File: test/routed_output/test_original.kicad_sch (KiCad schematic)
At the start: 3 parts, among them U1 CP_Radial_D25.0mm_P10.00mm_Sn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, U2 R_Axial_DIN0207_L6.3mm_D2.5mm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, U3 R_Axial_DIN0207_L6.3mm_D2.5mm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

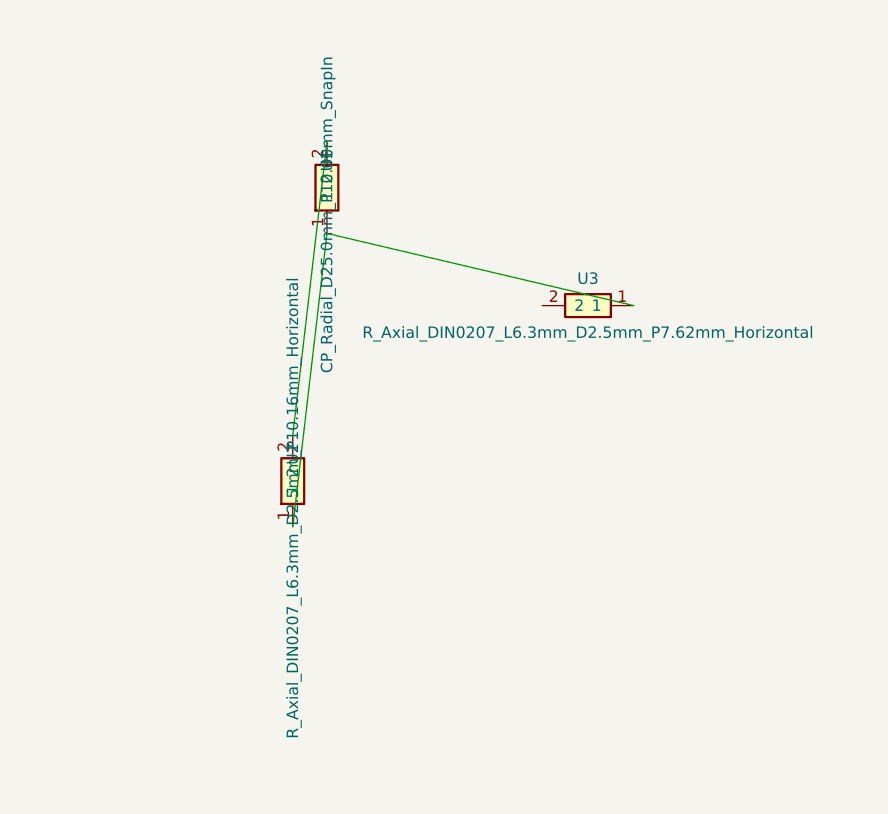
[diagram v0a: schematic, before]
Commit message: fix: schematic router - pin_map mapping + rotation formula alignment
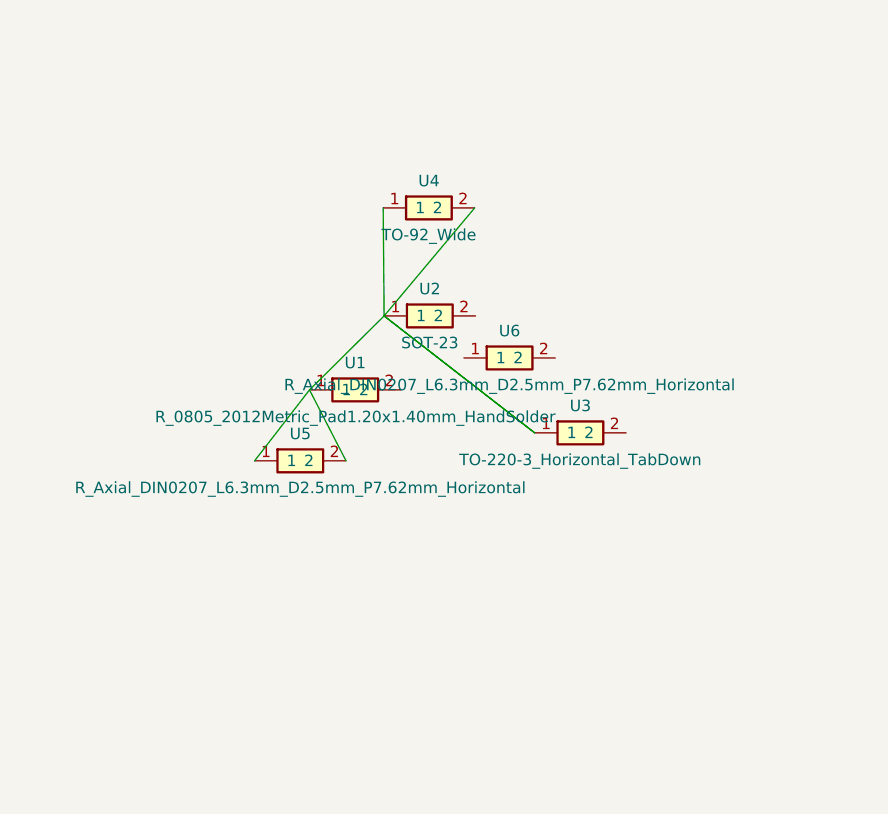
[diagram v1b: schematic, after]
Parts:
- removed U1: CP_Radial_D25.0mm_P10.00mm_SnapIn, 00_basic:CP_Radial_D25.0mm_P10.00mm_SnapIn, symbol 00_basic:C_Polarized
- removed U2: R_Axial_DIN0207_L6.3mm_D2.5mm_P10.16mm_Horizontal, 00_basic:R_Axial_DIN0207_L6.3mm_D2.5mm_P10.16mm_Horizontal, symbol 00_basic:R
- removed U3: R_Axial_DIN0207_L6.3mm_D2.5mm_P7.62mm_Horizontal, 00_basic:R_Axial_DIN0207_L6.3mm_D2.5mm_P7.62mm_Horizontal, symbol _placeholder:U3
- added U1: R_0805_2012Metric_Pad1.20x1.40mm_HandSolder, 00_basic:R_0805_2012Metric_Pad1.20x1.40mm_HandSolder, symbol RE_passive:R
- added U2: SOT-23, RE_active:SOT-23, symbol RE_active:Q_NPN
- added U3: TO-220-3_Horizontal_TabDown, RE_active:TO-220-3_Horizontal_TabDown, symbol RE_active:Q_NMOS
- added U4: TO-92_Wide, RE_active:TO-92_Wide, symbol RE_active:Q_NPN
- added U5: R_Axial_DIN0207_L6.3mm_D2.5mm_P7.62mm_Horizontal, RE_passive_tht:R_Axial_DIN0207_L6.3mm_D2.5mm_P7.62mm_Horizontal, symbol _placeholder:U5
- added U6: R_Axial_DIN0207_L6.3mm_D2.5mm_P7.62mm_Horizontal, RE_passive_tht:R_Axial_DIN0207_L6.3mm_D2.5mm_P7.62mm_Horizontal, symbol _placeholder:U6
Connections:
- new net: U1.1, U2.1, U3.1, U4.1, U4.2, U5.1, U5.2
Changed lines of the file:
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@@
   (paper "A4")
   (symbol
-    (lib_id "00_basic:C_Polarized")
-    (at 135.90 88.70 90)
+    (lib_id "RE_passive:R")
+    (at 139.04 111.17 0)
     (unit 1)
     (exclude_from_sim no)
@@
     (on_board yes)
     (dnp no)
-    (property "Reference" "U1" (at 135.90 85.70 0)
+    (property "Reference" "U1" (at 139.04 108.17 0)
       (effects (font (size 1.27 1.27)))
     )
-    (property "Value" "CP_Radial_D25.0mm_P10.00mm_SnapIn" (at 135.90 91.70 0)
+    (property "Value" "R_0805_2012Metric_Pad1.20x1.40mm_HandSolder" (at 139.04 114.17 0)
       (effects (font (size 1.27 1.27)))
     )
-    (property "Footprint" "00_basic:CP_Radial_D25.0mm_P10.00mm_SnapIn" (at 135.90 93.70 0)
+    (property "Footprint" "00_basic:R_0805_2012Metric_Pad1.20x1.40mm_HandSolder" (at 139.04 116.17 0)
       (effects (font (size 1.27 1.27)) hide)
     )
@@
   )
   (symbol
-    (lib_id "00_basic:R")
-    (at 132.10 121.30 90)
+    (lib_id "RE_active:Q_NPN")
+    (at 147.33 102.95 0)
     (unit 1)
     (exclude_from_sim no)
@@
     (on_board yes)
     (dnp no)
-    (property "Reference" "U2" (at 132.10 118.30 0)
+    (property "Reference" "U2" (at 147.33 99.95 0)
       (effects (font (size 1.27 1.27)))
     )
-    (property "Value" "R_Axial_DIN0207_L6.3mm_D2.5mm_P10.16mm_Horizontal" (at 132.10 124.30 0)
+    (property "Value" "SOT-23" (at 147.33 105.95 0)
       (effects (font (size 1.27 1.27)))
     )
-    (property "Footprint" "00_basic:R_Axial_DIN0207_L6.3mm_D2.5mm_P10.16mm_Horizontal" (at 132.10 126.30 0)
+    (property "Footprint" "RE_active:SOT-23" (at 147.33 107.95 0)
       (effects (font (size 1.27 1.27)) hide)
     )
@@
   )
   (symbol
-    (lib_id "_placeholder:U3")
-    (at 164.90 101.80 180)
+    (lib_id "RE_active:Q_NMOS")
+    (at 164.06 115.94 0)
     (unit 1)
     (exclude_from_sim no)
@@
     (on_board yes)
     (dnp no)
-    (property "Reference" "U3" (at 164.90 98.80 0)
+    (property "Reference" "U3" (at 164.06 112.94 0)
       (effects (font (size 1.27 1.27)))
     )
-    (property "Value" "R_Axial_DIN0207_L6.3mm_D2.5mm_P7.62mm_Horizontal" (at 164.90 104.80 0)
+    (property "Value" "TO-220-3_Horizontal_TabDown" (at 164.06 118.94 0)
       (effects (font (size 1.27 1.27)))
     )
-    (property "Footprint" "00_basic:R_Axial_DIN0207_L6.3mm_D2.5mm_P7.62mm_Horizontal" (at 164.90 106.80 0)
+    (property "Footprint" "RE_active:TO-220-3_Horizontal_TabDown" (at 164.06 120.94 0)
       (effects (font (size 1.27 1.27)) hide)
     )
@@
     )
   )
-  (wire (pts (xy 132.10 126.38) (xy 135.90 93.78))
+  (symbol
+    (lib_id "RE_active:Q_NPN")
+    (at 147.23 90.95 0)
+    (unit 1)
+    (exclude_from_sim no)
+    (in_bom yes)
+    (on_board yes)
+    (dnp no)
+    (property "Reference" "U4" (at 147.23 87.95 0)
+      (effects (font (size 1.27 1.27)))
+    )
+    (property "Value" "TO-92_Wide" (at 147.23 93.95 0)
+      (effects (font (size 1.27 1.27)))
+    )
+    (property "Footprint" "RE_active:TO-92_Wide" (at 147.23 95.95 0)
+      (effects (font (size 1.27 1.27)) hide)
+    )
+    (instances
+      (project ""
+        (path "/"
+          (reference "U4")
+          (unit 1)
+        )
+      )
+    )
+  )
+  (symbol
+    (lib_id "_placeholder:U5")
+    (at 132.94 119.05 0)
+    (unit 1)
+    (exclude_from_sim no)
+    (in_bom yes)
+    (on_board yes)
+    (dnp no)
+    (property "Reference" "U5" (at 132.94 116.05 0)
+      (effects (font (size 1.27 1.27)))
+    )
+    (property "Value" "R_Axial_DIN0207_L6.3mm_D2.5mm_P7.62mm_Horizontal" (at 132.94 122.05 0)
+      (effects (font (size 1.27 1.27)))
+    )
+    (property "Footprint" "RE_passive_tht:R_Axial_DIN0207_L6.3mm_D2.5mm_P7.62mm_Horizontal" (at 132.94 124.05 0)
+      (effects (font (size 1.27 1.27)) hide)
+    )
+    (instances
+      (project ""
+        (path "/"
+          (reference "U5")
+          (unit 1)
+        )
+      )
+    )
+  )
+  (symbol
+    (lib_id "_placeholder:U6")
+    (at 156.19 107.62 0)
+    (unit 1)
+    (exclude_from_sim no)
+    (in_bom yes)
+    (on_board yes)
+    (dnp no)
+    (property "Reference" "U6" (at 156.19 104.62 0)
+      (effects (font (size 1.27 1.27)))
+    )
+    (property "Value" "R_Axial_DIN0207_L6.3mm_D2.5mm_P7.62mm_Horizontal" (at 156.19 110.62 0)
+      (effects (font (size 1.27 1.27)))
+    )
+    (property "Footprint" "RE_passive_tht:R_Axial_DIN0207_L6.3mm_D2.5mm_P7.62mm_Horizontal" (at 156.19 112.62 0)
+      (effects (font (size 1.27 1.27)) hide)
+    )
+    (instances
+      (project ""
+        (path "/"
+          (reference "U6")
+          (unit 1)
+        )
+      )
+    )
+  )
+  (wire (pts (xy 152.31 90.95) (xy 142.25 102.95))
     (stroke (width 0) (type default))
   )
-  (wire (pts (xy 132.10 116.22) (xy 135.90 83.62))
+  (wire (pts (xy 142.25 102.95) (xy 158.98 115.94))
     (stroke (width 0) (type default))
   )
-  (wire (pts (xy 135.90 93.78) (xy 169.98 101.80))
+  (wire (pts (xy 142.25 102.95) (xy 158.98 115.94))
     (stroke (width 0) (type default))
   )
+  (wire (pts (xy 142.25 102.95) (xy 142.15 90.95))
+    (stroke (width 0) (type default))
+  )
+  (wire (pts (xy 133.96 111.17) (xy 142.25 102.95))
+    (stroke (width 0) (type default))
+  )
+  (wire (pts (xy 133.96 111.17) (xy 127.86 119.05))
+    (stroke (width 0) (type default))
+  )
+  (wire (pts (xy 133.96 111.17) (xy 138.02 119.05))
+    (stroke (width 0) (type default))
+  )

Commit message: backup
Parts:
- added U7: CP_Radial_D30.0mm_P10.00mm_SnapIn, RE_passive_tht:CP_Radial_D30.0mm_P10.00mm_SnapIn, symbol RE_passive:C_Polarized
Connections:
- net at U3.2: now also U7.2
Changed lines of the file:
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@@
   (symbol
     (lib_id "RE_passive:R")
-    (at 139.04 111.17 0)
-    (unit 1)
-    (exclude_from_sim no)
-    (in_bom yes)
-    (on_board yes)
-    (dnp no)
-    (property "Reference" "U1" (at 139.04 108.17 0)
-      (effects (font (size 1.27 1.27)))
-    )
-    (property "Value" "R_0805_2012Metric_Pad1.20x1.40mm_HandSolder" (at 139.04 114.17 0)
-      (effects (font (size 1.27 1.27)))
-    )
-    (property "Footprint" "00_basic:R_0805_2012Metric_Pad1.20x1.40mm_HandSolder" (at 139.04 116.17 0)
-      (effects (font (size 1.27 1.27)) hide)
-    )
-    (instances
-      (project ""
-        (path "/"
+    (at 139.04 127.96 0)
+    (unit 1)
+    (exclude_from_sim no)
+    (in_bom yes)
+    (on_board yes)
+    (dnp no)
+    (property "Reference" "U1" (at 139.04 124.96 0)
+      (effects (font (size 1.27 1.27)))
+    )
+    (property "Value" "R_0805_2012Metric_Pad1.20x1.40mm_HandSolder" (at 139.04 130.96 0)
+      (effects (font (size 1.27 1.27)))
+    )
+    (property "Footprint" "00_basic:R_0805_2012Metric_Pad1.20x1.40mm_HandSolder" (at 139.04 132.96 0)
+      (effects (font (size 1.27 1.27)) hide)
+    )
+    (instances
+      (project ""
+        (path "/76b0d100-f5a4-4cb0-a1b7-3defec0bed4b"
           (reference "U1")
           (unit 1)
@@
   (symbol
     (lib_id "RE_active:Q_NPN")
-    (at 147.33 102.95 0)
-    (unit 1)
-    (exclude_from_sim no)
-    (in_bom yes)
-    (on_board yes)
-    (dnp no)
-    (property "Reference" "U2" (at 147.33 99.95 0)
-      (effects (font (size 1.27 1.27)))
-    )
-    (property "Value" "SOT-23" (at 147.33 105.95 0)
-      (effects (font (size 1.27 1.27)))
-    )
-    (property "Footprint" "RE_active:SOT-23" (at 147.33 107.95 0)
-      (effects (font (size 1.27 1.27)) hide)
-    )
-    (instances
-      (project ""
-        (path "/"
+    (at 147.33 119.74 0)
+    (unit 1)
+    (exclude_from_sim no)
+    (in_bom yes)
+    (on_board yes)
+    (dnp no)
+    (property "Reference" "U2" (at 147.33 116.74 0)
+      (effects (font (size 1.27 1.27)))
+    )
+    (property "Value" "SOT-23" (at 147.33 122.74 0)
+      (effects (font (size 1.27 1.27)))
+    )
+    (property "Footprint" "RE_active:SOT-23" (at 147.33 124.74 0)
+      (effects (font (size 1.27 1.27)) hide)
+    )
+    (instances
+      (project ""
+        (path "/76b0d100-f5a4-4cb0-a1b7-3defec0bed4b"
           (reference "U2")
           (unit 1)
@@
   (symbol
     (lib_id "RE_active:Q_NMOS")
-    (at 164.06 115.94 0)
-    (unit 1)
-    (exclude_from_sim no)
-    (in_bom yes)
-    (on_board yes)
-    (dnp no)
-    (property "Reference" "U3" (at 164.06 112.94 0)
-      (effects (font (size 1.27 1.27)))
-    )
-    (property "Value" "TO-220-3_Horizontal_TabDown" (at 164.06 118.94 0)
-      (effects (font (size 1.27 1.27)))
-    )
-    (property "Footprint" "RE_active:TO-220-3_Horizontal_TabDown" (at 164.06 120.94 0)
-      (effects (font (size 1.27 1.27)) hide)
-    )
-    (instances
-      (project ""
-        (path "/"
+    (at 164.06 132.73 0)
+    (unit 1)
+    (exclude_from_sim no)
+    (in_bom yes)
+    (on_board yes)
+    (dnp no)
+    (property "Reference" "U3" (at 164.06 129.73 0)
+      (effects (font (size 1.27 1.27)))
+    )
+    (property "Value" "TO-220-3_Horizontal_TabDown" (at 164.06 135.73 0)
+      (effects (font (size 1.27 1.27)))
+    )
+    (property "Footprint" "RE_active:TO-220-3_Horizontal_TabDown" (at 164.06 137.73 0)
+      (effects (font (size 1.27 1.27)) hide)
+    )
+    (instances
+      (project ""
+        (path "/76b0d100-f5a4-4cb0-a1b7-3defec0bed4b"
           (reference "U3")
           (unit 1)
@@
   (symbol
     (lib_id "RE_active:Q_NPN")
-    (at 147.23 90.95 0)
-    (unit 1)
-    (exclude_from_sim no)
-    (in_bom yes)
-    (on_board yes)
-    (dnp no)
-    (property "Reference" "U4" (at 147.23 87.95 0)
-      (effects (font (size 1.27 1.27)))
-    )
-    (property "Value" "TO-92_Wide" (at 147.23 93.95 0)
-      (effects (font (size 1.27 1.27)))
-    )
-    (property "Footprint" "RE_active:TO-92_Wide" (at 147.23 95.95 0)
-      (effects (font (size 1.27 1.27)) hide)
-    )
-    (instances
-      (project ""
-        (path "/"
+    (at 147.23 107.75 0)
+    (unit 1)
+    (exclude_from_sim no)
+    (in_bom yes)
+    (on_board yes)
+    (dnp no)
+    (property "Reference" "U4" (at 147.23 104.75 0)
+      (effects (font (size 1.27 1.27)))
+    )
+    (property "Value" "TO-92_Wide" (at 147.23 110.75 0)
+      (effects (font (size 1.27 1.27)))
+    )
+    (property "Footprint" "RE_active:TO-92_Wide" (at 147.23 112.75 0)
+      (effects (font (size 1.27 1.27)) hide)
+    )
+    (instances
+      (project ""
+        (path "/76b0d100-f5a4-4cb0-a1b7-3defec0bed4b"
           (reference "U4")
           (unit 1)
@@
   (symbol
     (lib_id "_placeholder:U5")
-    (at 132.94 119.05 0)
-    (unit 1)
-    (exclude_from_sim no)
-    (in_bom yes)
-    (on_board yes)
-    (dnp no)
-    (property "Reference" "U5" (at 132.94 116.05 0)
-      (effects (font (size 1.27 1.27)))
-    )
-    (property "Value" "R_Axial_DIN0207_L6.3mm_D2.5mm_P7.62mm_Horizontal" (at 132.94 122.05 0)
-      (effects (font (size 1.27 1.27)))
-    )
-    (property "Footprint" "RE_passive_tht:R_Axial_DIN0207_L6.3mm_D2.5mm_P7.62mm_Horizontal" (at 132.94 124.05 0)
-      (effects (font (size 1.27 1.27)) hide)
-    )
-    (instances
-      (project ""
-        (path "/"
+    (at 132.94 135.84 0)
+    (unit 1)
+    (exclude_from_sim no)
+    (in_bom yes)
+    (on_board yes)
+    (dnp no)
+    (property "Reference" "U5" (at 132.94 132.84 0)
+      (effects (font (size 1.27 1.27)))
+    )
+    (property "Value" "R_Axial_DIN0207_L6.3mm_D2.5mm_P7.62mm_Horizontal" (at 132.94 138.84 0)
+      (effects (font (size 1.27 1.27)))
+    )
+    (property "Footprint" "RE_passive_tht:R_Axial_DIN0207_L6.3mm_D2.5mm_P7.62mm_Horizontal" (at 132.94 140.84 0)
+      (effects (font (size 1.27 1.27)) hide)
+    )
+    (instances
+      (project ""
+        (path "/76b0d100-f5a4-4cb0-a1b7-3defec0bed4b"
           (reference "U5")
           (unit 1)
@@
   (symbol
     (lib_id "_placeholder:U6")
-    (at 156.19 107.62 0)
-    (unit 1)
-    (exclude_from_sim no)
-    (in_bom yes)
-    (on_board yes)
-    (dnp no)
-    (property "Reference" "U6" (at 156.19 104.62 0)
-      (effects (font (size 1.27 1.27)))
-    )
-    (property "Value" "R_Axial_DIN0207_L6.3mm_D2.5mm_P7.62mm_Horizontal" (at 156.19 110.62 0)
-      (effects (font (size 1.27 1.27)))
-    )
-    (property "Footprint" "RE_passive_tht:R_Axial_DIN0207_L6.3mm_D2.5mm_P7.62mm_Horizontal" (at 156.19 112.62 0)
-      (effects (font (size 1.27 1.27)) hide)
-    )
-    (instances
-      (project ""
-        (path "/"
+    (at 156.19 124.41 0)
+    (unit 1)
+    (exclude_from_sim no)
+    (in_bom yes)
+    (on_board yes)
+    (dnp no)
+    (property "Reference" "U6" (at 156.19 121.41 0)
+      (effects (font (size 1.27 1.27)))
+    )
+    (property "Value" "R_Axial_DIN0207_L6.3mm_D2.5mm_P7.62mm_Horizontal" (at 156.19 127.41 0)
+      (effects (font (size 1.27 1.27)))
+    )
+    (property "Footprint" "RE_passive_tht:R_Axial_DIN0207_L6.3mm_D2.5mm_P7.62mm_Horizontal" (at 156.19 129.41 0)
+      (effects (font (size 1.27 1.27)) hide)
+    )
+    (instances
+      (project ""
+        (path "/76b0d100-f5a4-4cb0-a1b7-3defec0bed4b"
           (reference "U6")
           (unit 1)
@@
     )
   )
-  (wire (pts (xy 152.31 90.95) (xy 142.25 102.95))
-    (stroke (width 0) (type default))
-  )
-  (wire (pts (xy 142.25 102.95) (xy 158.98 115.94))
-    (stroke (width 0) (type default))
-  )
-  (wire (pts (xy 142.25 102.95) (xy 158.98 115.94))
-    (stroke (width 0) (type default))
-  )
-  (wire (pts (xy 142.25 102.95) (xy 142.15 90.95))
-    (stroke (width 0) (type default))
-  )
-  (wire (pts (xy 133.96 111.17) (xy 142.25 102.95))
-    (stroke (width 0) (type default))
-  )
-  (wire (pts (xy 133.96 111.17) (xy 127.86 119.05))
-    (stroke (width 0) (type default))
-  )
-  (wire (pts (xy 133.96 111.17) (xy 138.02 119.05))
-    (stroke (width 0) (type default))
-  )
+  (symbol
+    (lib_id "RE_passive:C_Polarized")
+    (at 157.54 74.16 0)
+    (unit 1)
+    (exclude_from_sim no)
+    (in_bom yes)
+    (on_board yes)
+    (dnp no)
+    (property "Reference" "U7" (at 157.54 71.16 0)
+      (effects (font (size 1.27 1.27)))
+    )
+    (property "Value" "CP_Radial_D30.0mm_P10.00mm_SnapIn" (at 157.54 77.16 0)
+      (effects (font (size 1.27 1.27)))
+    )
+    (property "Footprint" "RE_passive_tht:CP_Radial_D30.0mm_P10.00mm_SnapIn" (at 157.54 79.16 0)
+      (effects (font (size 1.27 1.27)) hide)
+    )
+    (instances
+      (project ""
+        (path "/76b0d100-f5a4-4cb0-a1b7-3defec0bed4b"
+          (reference "U7")
+          (unit 1)
+        )
+      )
+    )
+  )
+  (wire (pts (xy 152.31 107.75) (xy 142.25 119.74))
+    (stroke (width 0) (type default))
+  )
+  (wire (pts (xy 142.25 119.74) (xy 158.98 132.73))
+    (stroke (width 0) (type default))
+  )
+  (wire (pts (xy 142.25 119.74) (xy 158.98 132.73))
+    (stroke (width 0) (type default))
+  )
+  (wire (pts (xy 142.25 119.74) (xy 142.15 107.75))
+    (stroke (width 0) (type default))
+  )
+  (wire (pts (xy 133.96 127.96) (xy 142.25 119.74))
+    (stroke (width 0) (type default))
+  )
+  (wire (pts (xy 133.96 127.96) (xy 127.86 135.84))
+    (stroke (width 0) (type default))
+  )
+  (wire (pts (xy 133.96 127.96) (xy 138.02 135.84))
+    (stroke (width 0) (type default))
+  )
+  (wire (pts (xy 169.14 132.73) (xy 162.62 74.16))
+    (stroke (width 0) (type default))
+  )
